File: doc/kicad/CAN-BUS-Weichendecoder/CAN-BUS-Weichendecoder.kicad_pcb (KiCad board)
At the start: 2 copper layers, 25 parts, among them J1 RJ45_LED_Shielded, J2 RJ45_Shielded, K1 HFD2_005-S-L2-D, U1 ULN2803A, U2 ULN2803A, U3 PCF8574, U4 PCF8574, U5 PCF8574, U6 ULN2803A, U7 ULN2803A, U8 ULN2803A

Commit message: Aktueller Stand
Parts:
- moved K1 187.6 mm to (201.9, 52.1)
- moved U4 125.7 mm to (81.3, 100.3), turned to 90 degrees
- moved U7 106.4 mm to (99.1, 109.2), turned to 270 degrees
- moved C2 96.3 mm to (135.9, 95.3), turned to 270 degrees
- moved U5 84.9 mm to (111.8, 100.3), turned to 90 degrees
- moved U8 70.0 mm to (129.5, 109.2), turned to 270 degrees
- moved C1 55.8 mm to (77.5, 95.2), turned to 270 degrees
- moved U3 48.3 mm to (142.2, 100.3), turned to 90 degrees
- moved U6 46.9 mm to (160.0, 109.2), turned to 270 degrees
- moved JP2 46.2 mm to (92.7, 82.8)
- moved JP3 46.2 mm to (86.2, 82.8)
- moved JP4 46.2 mm to (89.5, 82.8)
- moved R2 46.2 mm to (87.6, 71.8)
- moved R1 46.2 mm to (91.2, 69.3)
- moved R3 46.2 mm to (87.6, 69.3)
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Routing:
- net GND: track 212.0 -> 320.7 mm
- net +5V: track 94.6 -> 165.5 mm
- net Net-(A1-Pad24): track 83.1 -> 139.2 mm
- net Net-(A1-Pad23): track 83.1 -> 136.7 mm
- net Net-(A1-Pad22): track 0.00 -> 40.7 mm
- net Net-(A1-Pad21): track 0.00 -> 40.7 mm
- net Net-(U3-Pad9): track 1.59 -> 32.1 mm
- net Net-(U3-Pad12): track 1.59 -> 20.7 mm
- net Net-(U3-Pad11): track 1.59 -> 20.7 mm
- net Net-(U3-Pad10): track 1.59 -> 20.7 mm
- net Net-(U3-Pad4): track 0.00 -> 18.9 mm
- net Net-(U3-Pad7): track 0.00 -> 16.8 mm
- net Net-(U3-Pad5): track 0.00 -> 11.0 mm
- net Net-(U3-Pad6): track 0.00 -> 8.89 mm
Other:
- board outline added: 158.8 x 124.5 mm

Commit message: Platine weiterentwickelt, aktueller Arbeitsstand
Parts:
- moved U6 17.0 mm to (175.3, 116.8)
- moved U3 10.8 mm to (149.9, 108.0)
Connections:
- A1 pad 13: Net-(A1-Pad13) -> (no net)
- A1 pad 14: Net-(A1-Pad14) -> (no net)
- A1 pad 15: Net-(A1-Pad15) -> (no net)
- A1 pad 16: Net-(A1-Pad16) -> (no net)
- A1 pad 5: Net-(A1-Pad5) -> (no net)
- Shield1 pad 1: +5V -> (no net)
- Shield1 pad 2: GND -> (no net)
- Shield1 pad 3: Net-(A1-Pad13) -> (no net)
- Shield1 pad 4: Net-(A1-Pad15) -> (no net)
- Shield1 pad 5: Net-(A1-Pad14) -> (no net)
- Shield1 pad 6: Net-(A1-Pad16) -> (no net)
- Shield1 pad 7: Net-(A1-Pad5) -> (no net)
- U6 pad 1: Net-(U3-Pad4) -> Net-(U3-Pad9)
- U6 pad 2: Net-(U3-Pad5) -> Net-(U3-Pad10)
- U6 pad 3: Net-(U3-Pad6) -> Net-(U3-Pad11)
- U6 pad 4: Net-(U3-Pad7) -> Net-(U3-Pad12)
- U6 pad 5: Net-(U3-Pad9) -> Net-(U3-Pad7)
- U6 pad 6: Net-(U3-Pad10) -> Net-(U3-Pad6)
- U6 pad 7: Net-(U3-Pad11) -> Net-(U3-Pad5)
- U6 pad 8: Net-(U3-Pad12) -> Net-(U3-Pad4)
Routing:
- net (no net): track 0.00 -> 197.6 mm
- net Net-(A1-Pad5): track 63.9 -> 0.00 mm
- net Net-(A1-Pad13): track 37.1 -> 0.00 mm
- net Net-(A1-Pad14): track 35.2 -> 0.00 mm
- net Net-(A1-Pad15): track 30.9 -> 0.00 mm
- net Net-(A1-Pad16): track 26.7 -> 0.00 mm
- net GND: track 320.7 -> 303.4 mm
- net Net-(U3-Pad4): track 18.9 -> 8.89 mm
- net Net-(U3-Pad9): track 32.1 -> 23.4 mm
- net Net-(U3-Pad7): track 16.8 -> 8.89 mm
- net Net-(U3-Pad12): track 20.7 -> 27.7 mm
- net Net-(U3-Pad11): track 20.7 -> 27.7 mm
- net Net-(U3-Pad10): track 20.7 -> 25.9 mm
- net Net-(U3-Pad5): track 11.0 -> 8.89 mm

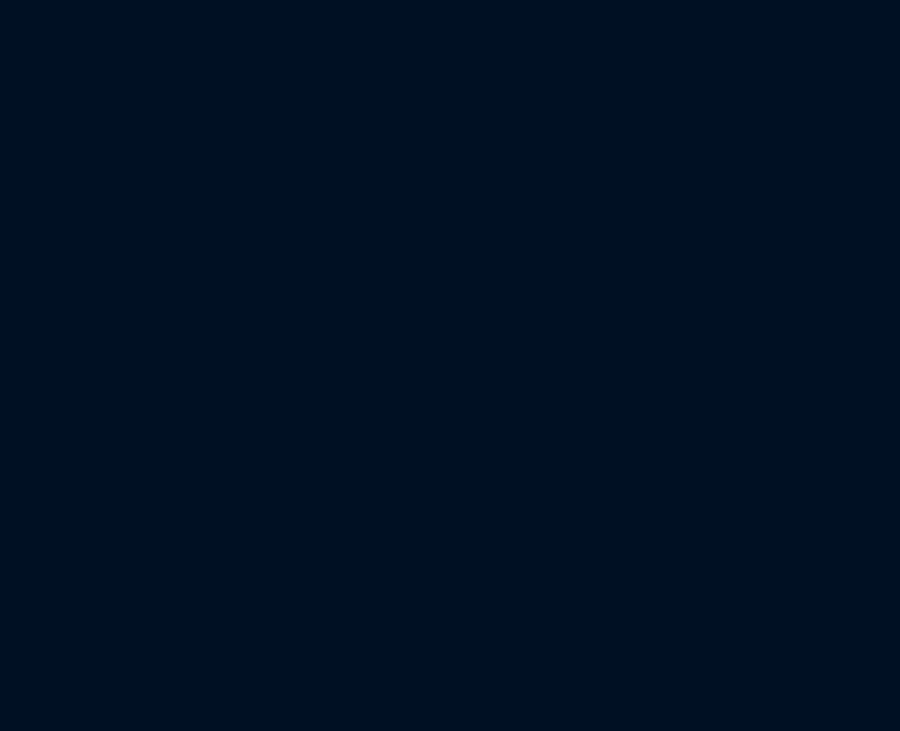
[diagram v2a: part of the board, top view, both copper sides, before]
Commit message: Auch die Bedruckung jetzt auf beiden Seiten, Platine jetzt komplett für Links und Rechts
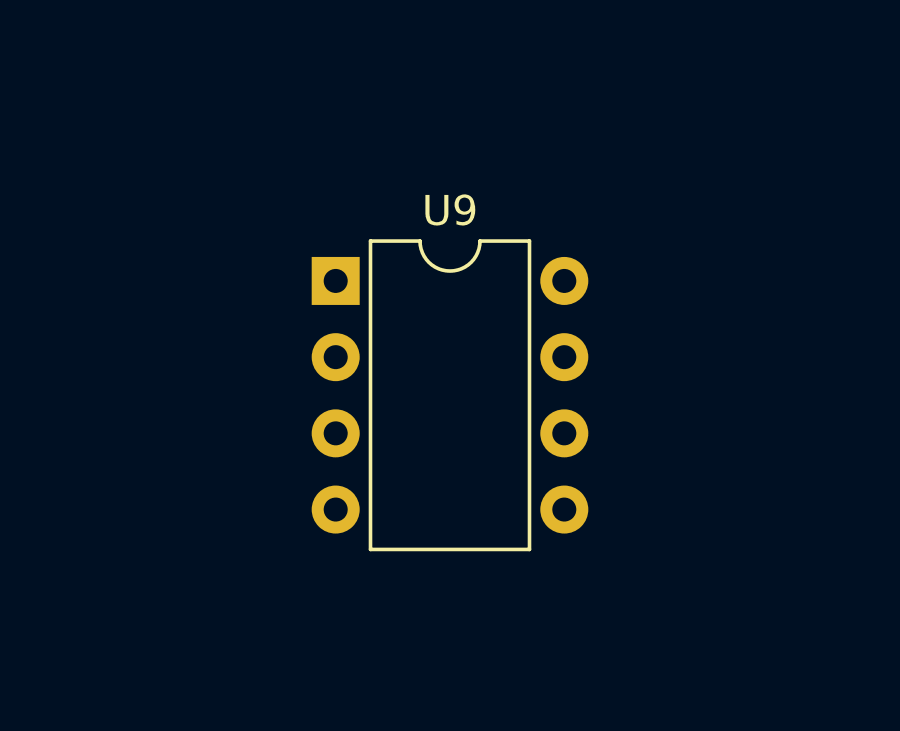
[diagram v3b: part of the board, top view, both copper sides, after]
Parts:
- added U9: 6N136, Package_DIP:DIP-8_W7.62mm, F.Cu at (39.4, 34.3)
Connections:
- A1 pad 6: (no net) -> Net-(A1-Pad6)

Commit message: Wago-Klemmen 250-140x verwendet
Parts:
- removed K1: HFD2_005-S-L2-D, HFD2_005-S-L2-D:HFD2005SL2D
- removed Shield1: CAN-BUS_MODULE_TJA1050, kicad-lib:MCP2515_CAN_MODULE_BY0-10
- removed the U9 at (39.4, 34.3)
- added C1: 2200µ/35V, Capacitors_THT:CP_Radial_D16.0mm_P7.50mm, F.Cu at (-199.9, -160.5)
- added C2: 2200µF/35V, Capacitors_THT:CP_Radial_D16.0mm_P7.50mm, F.Cu at (-217.6, -160.5)
- added D1: 1N4004, Diodes_THT:D_DO-15_P10.16mm_Horizontal, F.Cu at (-31.5, -114.7)
- added D2: B40C1500A, Diodes_THT:Diode_Bridge_DIP-4_W7.62mm_P5.08mm, F.Cu at (-17.8, -114.8)
- added D3: B140C1000A, Diodes_THT:Diode_Bridge_DIP-4_W7.62mm_P5.08mm, F.Cu at (15.7, -67.3)
- added DS1001: DC-10SGWA, Kingbright-LED:DIPS750W80P254L2540H825Q20N, F.Cu at (160.0, 55.9)
- added J1: 250-1404, Wago:250-1404, F.Cu at (76.2, 3.81)
- added J1001: Conn_01x02_Female, Pin_Headers:Pin_Header_Straight_1x02_Pitch2.54mm, F.Cu at (223.5, 72.4)
- added J1003: Conn_01x07_Female, Pin_Headers:Pin_Header_Straight_1x07_Pitch2.54mm, F.Cu at (69.8, 58.4)
- added J11: 250-1406, Wago:CONN_250-1406_WAG, F.Cu at (124.5, 129.5)
- added J12: Wago 250-1406, Wago:CONN_250-1406_WAG, F.Cu at (104.1, 129.5)
- added J13: Wago 250-1406, Wago:CONN_250-1406_WAG, F.Cu at (83.8, 129.5)
- added J14: Wago 250-1406, Wago:CONN_250-1406_WAG, F.Cu at (63.5, 129.5)
- added J2: 250-1404, Wago:250-1404, F.Cu at (88.9, 3.81)
- added J3: 250-1404, Wago:250-1404, F.Cu at (101.6, 3.81)
- added J31: 2604-1102, CONN_2604-1102_4_WAG, F.Cu at (-191.8, 14.6)
- added J4: 250-1404, Wago:250-1404, F.Cu at (114.3, 3.81)
- added J41: 2604-1102, CONN_2604-1102_4_WAG, F.Cu at (-175.8, 14.6)
- added J5: 250-1404, Wago:250-1404, F.Cu at (127.0, 3.81)
- added JP1: JP3, Pin_Headers:Pin_Header_Straight_1x02_Pitch2.54mm, F.Cu at (92.7, 82.8)
- added JP11: Jumper, Pin_Headers:Pin_Header_Straight_1x02_Pitch2.54mm, F.Cu at (219.7, 36.8)
- added R1: 1k5, Resistors_THT:R_Axial_DIN0207_L6.3mm_D2.5mm_P7.62mm_Horizontal, F.Cu at (4.89, -60.3)
- added R2: 10K, Resistors_THT:R_Axial_DIN0207_L6.3mm_D2.5mm_P7.62mm_Horizontal, F.Cu at (15.7, -72.0)
- added R7: 1k, Resistors_THT:R_Array_SIP6, F.Cu at (175.3, 53.3)
- added R8: 1k, Resistors_THT:R_Array_SIP6, F.Cu at (175.3, 81.3)
- added Shield1001: CAN-BUS_MODULE_TJA1050, CAN-BUS-MODULE:MCP2515_CAN_MODULE_BY0-10, F.Cu at (67.3, 52.1)
- added U10: TSR_1-24120, Converters_DCDC_ACDC:DCDC-Conv_TRACO_TSR-1, F.Cu at (-218.4, -145.3)
- added U1001: 6N136, Package_DIP:DIP-8_W7.62mm, F.Cu at (4.94, -72.1)
- added U11: TSR_1-2450, Converters_DCDC_ACDC:DCDC-Conv_TRACO_TSR-1, F.Cu at (-205.0, -145.3)
- J22: renamed from J2; value RJ45_Shielded -> J22
- JP2: value JP3 -> JP1; footprint Connectors:GS2 -> Pin_Headers:Pin_Header_Straight_1x02_Pitch2.54mm
- JP3: value JP1 -> JP2; footprint Connectors:GS2 -> Pin_Headers:Pin_Header_Straight_1x02_Pitch2.54mm
- JP4: value JP2 -> Jumper; footprint Connectors:GS2 -> Pin_Headers:Pin_Header_Straight_1x02_Pitch2.54mm
- moved JP4 264.2 mm to (-115.6, -83.8)
- moved U9 58.4 mm to (71.1, 109.2)
- moved U7 48.9 mm to (127.0, 109.2)
- moved U6 46.6 mm to (66.0, 91.4), turned to 270 degrees
- moved U4 41.6 mm to (109.2, 99.1)
- moved C1002 14.0 mm to (149.9, 94.0)
- moved R1007 11.6 mm to (134.6, 83.8)
- moved R1008 10.2 mm to (133.3, 90.2)
- moved JP2 6.50 mm to (86.2, 82.8)
- moved C1001 6.48 mm to (71.1, 94.0)
- moved C1003 4.04 mm to (101.6, 94.0)
- moved JP3 3.25 mm to (89.5, 82.8)
- moved U5 2.84 mm to (78.7, 99.1)
- renumbered C1 to C1001, C2 to C1002, C3 to C1003, J1 to J21, R4 to R1007, R5 to R1008, R6 to R3, R1 to R4, R3 to R5, R2 to R6, A1 to U1, U1 to U2, U2 to U3, U3 to U4, U4 to U5, U5 to U6, U6 to U7, U7 to U8, U8 to U9
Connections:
- JP2 pad 1: Net-(A1-Pad25) -> Net-(JP2-Pad1)
- JP4 pad 2: GND -> +12V
- R4 pad 1: Net-(A1-Pad25) -> Net-(JP1-Pad1)
- R4 pad 2: Net-(JP3-Pad1) -> Net-(JP2-Pad1)
- R5 pad 1: Net-(A1-Pad25) -> Net-(JP1-Pad1)
- R5 pad 2: Net-(JP4-Pad1) -> Net-(JP3-Pad1)
- R6 pad 2: Net-(A1-Pad25) -> Net-(JP1-Pad1)
- U1 pad 13: (no net) -> Net-(J1003-Pad3)
- U1 pad 14: (no net) -> Net-(J1003-Pad5)
- U1 pad 15: (no net) -> Net-(J1003-Pad4)
- U1 pad 16: (no net) -> Net-(J1003-Pad6)
- U1 pad 25: Net-(A1-Pad25) -> Net-(JP1-Pad1)
- U1 pad 5: (no net) -> Net-(J1003-Pad7)
- U2 pad 10: (no net) -> Net-(JP4-Pad1)
- U2 pad 11: (no net) -> Net-(J4-Pad3)
- U2 pad 12: (no net) -> Net-(J4-Pad2)
- U2 pad 13: (no net) -> Net-(J3-Pad3)
- U2 pad 14: (no net) -> Net-(J3-Pad2)
- U2 pad 15: (no net) -> Net-(J2-Pad3)
- U2 pad 16: (no net) -> Net-(J2-Pad2)
- U2 pad 17: (no net) -> Net-(J1-Pad3)
- U2 pad 18: (no net) -> Net-(J1-Pad2)
- U3 pad 10: (no net) -> Net-(JP4-Pad1)
- U3 pad 17: (no net) -> Net-(J5-Pad3)
- U3 pad 18: (no net) -> Net-(J5-Pad2)
- U7 pad 11: (no net) -> Net-(J12-Pad3)
- U7 pad 12: (no net) -> Net-(J12-Pad4)
- U7 pad 13: (no net) -> Net-(J12-Pad5)
- U7 pad 14: (no net) -> Net-(J11-Pad1)
- U7 pad 15: (no net) -> Net-(J11-Pad2)
- U7 pad 16: (no net) -> Net-(J11-Pad3)
- U7 pad 17: (no net) -> Net-(J11-Pad4)
- U7 pad 18: (no net) -> Net-(J11-Pad5)
- U8 pad 11: (no net) -> Net-(J14-Pad5)
- U8 pad 12: (no net) -> Net-(J13-Pad1)
- U8 pad 13: (no net) -> Net-(J13-Pad2)
- U8 pad 14: (no net) -> Net-(J13-Pad3)
- U8 pad 15: (no net) -> Net-(J13-Pad4)
- U8 pad 16: (no net) -> Net-(J13-Pad5)
- U8 pad 17: (no net) -> Net-(J12-Pad1)
- U8 pad 18: (no net) -> Net-(J12-Pad2)
- U9 pad 15: (no net) -> Net-(J14-Pad1)
- U9 pad 16: (no net) -> Net-(J14-Pad2)
- U9 pad 17: (no net) -> Net-(J14-Pad3)
- U9 pad 18: (no net) -> Net-(J14-Pad4)
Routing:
- net (no net): track 197.6 -> 0.00 mm
- net GND: track 303.4 -> 145.5 mm
- net Net-(R1007-Pad1): track 139.2 -> 0.00 mm
- net Net-(R1008-Pad1): track 136.7 -> 0.00 mm
- net +5V: track 165.5 -> 69.8 mm
- net Net-(J1003-Pad7): track 0.00 -> 52.5 mm
- net Net-(J1003-Pad3): track 0.00 -> 37.1 mm
- net Net-(J1003-Pad5): track 0.00 -> 35.2 mm
- net Net-(U6-Pad9): track 31.3 -> 0.00 mm
- net Net-(J1003-Pad4): track 0.00 -> 30.9 mm
- net Net-(U5-Pad9): track 30.6 -> 0.00 mm
- net Net-(U4-Pad12): track 27.7 -> 0.00 mm
- net Net-(U4-Pad11): track 27.7 -> 0.00 mm
- net Net-(U4-Pad10): track 25.9 -> 0.00 mm
- net Net-(U4-Pad9): track 23.4 -> 0.00 mm
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
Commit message: PCP weiterentwickelt
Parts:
- removed C1002: 100n, Capacitors_THT:C_Disc_D7.0mm_W2.5mm_P5.00mm
- removed J21: RJ45_LED_Shielded, Connectors:RJ45_TRANSFO
- removed R1007, R1008: 4k7, Resistors_SMD:R_0603
- removed R3: 1K, Resistors_SMD:R_0603
- added C4: 100n, Capacitors_THT:C_Disc_D7.0mm_W2.5mm_P5.00mm, F.Cu at (99.1, 92.7)
- added J15: Wago 250-1406, Wago:CONN_250-1406_WAG, F.Cu at (160.0, 127.0)
- added J23: J22, ASSMANN_WSW:A20042LPFS, F.Cu at (41.9, 127.0)
- added JP23: 12V CAN, Pin_Headers:Pin_Header_Straight_1x02_Pitch2.54mm, F.Cu at (57.1, 133.3)
- added JP41: DCC B, Pin_Headers:Pin_Header_Straight_1x02_Pitch2.54mm, F.Cu at (40.6, 90.2)
- added JP42: DCC A, Pin_Headers:Pin_Header_Straight_1x02_Pitch2.54mm, F.Cu at (44.5, 90.2)
- added R7: 4k7, Resistors_THT:R_Axial_DIN0207_L6.3mm_D2.5mm_P7.62mm_Horizontal, F.Cu at (114.3, 83.8)
- added R8: 4k7, Resistors_THT:R_Axial_DIN0207_L6.3mm_D2.5mm_P7.62mm_Horizontal, F.Cu at (114.3, 80.0)
- J22: footprint Connectors:RJ45_8 -> ASSMANN_WSW:A20042LPFS
- JP1: value JP3 -> Prog 1
- JP2: value JP1 -> Prog2
- JP3: value JP2 -> Prog3
- R4, R5, R6: footprint Resistors_SMD:R_0603 -> Resistors_THT:R_Axial_DIN0207_L6.3mm_D2.5mm_P7.62mm_Horizontal
- moved D3 265.2 mm to (-237.5, -146.1), turned to 270 degrees
- moved D2 224.6 mm to (-237.5, -161.3), turned to 270 degrees
- moved J31 183.3 mm to (-251.5, -158.8), turned to 270 degrees
- moved J22 97.6 mm to (41.9, 105.4)
- moved U9 94.0 mm to (165.1, 106.7)
- moved J14 76.2 mm to (139.7, 127.0)
- moved U6 71.5 mm to (137.2, 99.1), turned to 90 degrees
- moved C6 61.0 mm to (132.1, 92.7)
- moved D1 51.3 mm to (-2.54, -72.4), turned to 270 degrees
- moved J11 45.8 mm to (78.7, 127.0)
- moved U4 38.1 mm to (71.1, 99.1)
- moved J13 35.7 mm to (119.4, 127.0)
- moved C5 35.6 mm to (66.0, 92.7)
- moved U8 33.1 mm to (132.1, 106.7)
- moved U7 28.1 mm to (99.1, 106.7)
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- renumbered C1 to C10, C2 to C11, C1003 to C5, C1001 to C6, R8 to R10, R7 to R9
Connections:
- J11 pad 1: Net-(J11-Pad1) -> +5V
- J11 pad 6: +5V -> Net-(J11-Pad6)
- J12 pad 1: Net-(J12-Pad1) -> +5V
- J12 pad 6: +5V -> Net-(J12-Pad6)
- J13 pad 1: Net-(J13-Pad1) -> +5V
- J13 pad 6: +5V -> Net-(J13-Pad6)
- J14 pad 1: Net-(J14-Pad1) -> +5V
- J14 pad 6: +5V -> Net-(J14-Pad6)
- J22 pad 1: Net-(J21-Pad1) -> Net-(J22-Pad1)
- J22 pad 2: Net-(J21-Pad2) -> Net-(J22-Pad2)
- J22 pad 4: Net-(J21-Pad4) -> GND
- J22 pad 7: GND -> Net-(J22-Pad7)
- J22 pad 8: +5V -> Net-(J22-Pad8)
- J31 pad 1: Net-(D2-Pad3) -> Net-(D2-Pad2)
- J31 pad 2: Net-(D2-Pad3) -> Net-(D2-Pad2)
- J31 pad 3: Net-(D2-Pad2) -> Net-(D2-Pad3)
- J31 pad 4: Net-(D2-Pad2) -> Net-(D2-Pad3)
- J41 pad 1: Net-(D1-Pad2) -> Net-(J41-Pad1)
- J41 pad 2: Net-(D1-Pad2) -> Net-(J41-Pad1)
- J41 pad 3: Net-(J41-Pad3) -> Net-(D1-Pad2)
- J41 pad 4: Net-(J41-Pad3) -> Net-(D1-Pad2)
- R1 pad 2: Net-(J41-Pad3) -> Net-(J41-Pad1)
- Shield1001 pad H: Net-(J21-Pad1) -> Net-(J22-Pad8)
- Shield1001 pad L: Net-(J21-Pad2) -> Net-(J22-Pad7)
- U7 pad 1: Net-(U4-Pad9) -> Net-(U4-Pad12)
- U7 pad 11: Net-(J12-Pad3) -> Net-(J11-Pad2)
- U7 pad 12: Net-(J12-Pad4) -> Net-(J11-Pad3)
- U7 pad 13: Net-(J12-Pad5) -> Net-(J11-Pad4)
- U7 pad 14: Net-(J11-Pad1) -> Net-(J11-Pad5)
- U7 pad 15: Net-(J11-Pad2) -> Net-(J11-Pad6)
- U7 pad 16: Net-(J11-Pad3) -> Net-(J12-Pad2)
- U7 pad 17: Net-(J11-Pad4) -> Net-(J12-Pad3)
- U7 pad 18: Net-(J11-Pad5) -> Net-(J12-Pad4)
- U7 pad 2: Net-(U4-Pad10) -> Net-(U4-Pad11)
- U7 pad 3: Net-(U4-Pad11) -> Net-(U4-Pad10)
- U7 pad 4: Net-(U4-Pad12) -> Net-(U4-Pad9)
- U8 pad 1: Net-(U5-Pad4) -> Net-(U5-Pad12)
- U8 pad 11: Net-(J14-Pad5) -> Net-(J12-Pad5)
- U8 pad 12: Net-(J13-Pad1) -> Net-(J12-Pad6)
- U8 pad 17: Net-(J12-Pad1) -> Net-(J13-Pad6)
- U8 pad 18: Net-(J12-Pad2) -> Net-(J14-Pad2)
- U8 pad 2: Net-(U5-Pad5) -> Net-(U5-Pad11)
- U8 pad 3: Net-(U5-Pad6) -> Net-(U5-Pad10)
- U8 pad 4: Net-(U5-Pad7) -> Net-(U5-Pad9)
- U8 pad 5: Net-(U5-Pad9) -> Net-(U5-Pad7)
- U8 pad 6: Net-(U5-Pad10) -> Net-(U5-Pad6)
- U8 pad 7: Net-(U5-Pad11) -> Net-(U5-Pad5)
- U8 pad 8: Net-(U5-Pad12) -> Net-(U5-Pad4)
- U9 pad 1: Net-(U6-Pad4) -> Net-(U6-Pad12)
- U9 pad 11: (no net) -> Net-(J14-Pad3)
- U9 pad 12: (no net) -> Net-(J14-Pad4)
- U9 pad 13: (no net) -> Net-(J14-Pad5)
- U9 pad 14: (no net) -> Net-(J14-Pad6)
- U9 pad 15: Net-(J14-Pad1) -> Net-(J15-Pad2)
- U9 pad 16: Net-(J14-Pad2) -> Net-(J15-Pad3)
- U9 pad 17: Net-(J14-Pad3) -> Net-(J15-Pad4)
- U9 pad 18: Net-(J14-Pad4) -> Net-(J15-Pad5)
- U9 pad 2: Net-(U6-Pad5) -> Net-(U6-Pad11)
- U9 pad 3: Net-(U6-Pad6) -> Net-(U6-Pad10)
- U9 pad 4: Net-(U6-Pad7) -> Net-(U6-Pad9)
- U9 pad 5: Net-(U6-Pad9) -> Net-(U6-Pad7)
- U9 pad 6: Net-(U6-Pad10) -> Net-(U6-Pad6)
- U9 pad 7: Net-(U6-Pad11) -> Net-(U6-Pad5)
- U9 pad 8: Net-(U6-Pad12) -> Net-(U6-Pad4)
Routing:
- net GND: track 145.5 -> 450.3 mm
- net +5V: track 69.8 -> 230.7 mm
- net Net-(J22-Pad7): track 0.00 -> 103.2 mm, vias 0 -> 1
- net Net-(R7-Pad1): track 0.00 -> 100.0 mm
- net Net-(R8-Pad1): track 0.00 -> 99.2 mm
- net Net-(J22-Pad8): track 0.00 -> 91.2 mm, vias 0 -> 1
- net Net-(J22-Pad2): track 0.00 -> 61.9 mm, vias 0 -> 1
- net Net-(DS1001-Pad6): track 8.89 -> 70.8 mm
- net +12V: track 0.00 -> 61.9 mm
- net Net-(J22-Pad1): track 0.00 -> 60.8 mm, vias 0 -> 1
- net Net-(DS1001-Pad7): track 26.2 -> 86.0 mm
- net Net-(DS1001-Pad5): track 8.89 -> 67.2 mm
- net Net-(DS1001-Pad4): track 8.89 -> 63.6 mm
- net Net-(DS1001-Pad3): track 8.89 -> 60.0 mm
- net Net-(JP1-Pad1): track 0.00 -> 49.6 mm
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
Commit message: Erster kompletter Entwurf der Platine
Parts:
- removed C10: 2200µ/35V, Capacitors_THT:CP_Radial_D16.0mm_P7.50mm
- removed C11: 2200µF/35V, Capacitors_THT:CP_Radial_D16.0mm_P7.50mm
- removed D2: B40C1500A, Diodes_THT:Diode_Bridge_DIP-4_W7.62mm_P5.08mm
- removed D3: B140C1000A, Diodes_THT:Diode_Bridge_DIP-4_W7.62mm_P5.08mm
- removed U11: TSR_1-2450, Converters_DCDC_ACDC:DCDC-Conv_TRACO_TSR-1
- added D1001: DIODE, Diodes_THT:D_DO-15_P10.16mm_Horizontal, F.Cu at (77.5, 71.1)
- added D1002: LED, LEDs:LED_D3.0mm, F.Cu at (105.4, 74.9)
- added R20: 470, Resistors_THT:R_Axial_DIN0207_L6.3mm_D2.5mm_P7.62mm_Horizontal, F.Cu at (100.3, 72.4)
- J1003, Shield1001: moved to B.Cu
- J31: value 2604-1102 -> 12V DC
- U10: value TSR_1-24120 -> TSR_1-2450
- moved J31 395.5 mm to (68.6, 73.7)
- moved U10 374.7 mm to (87.6, 74.9)
- moved JP4 345.4 mm to (196.8, 63.5), turned to 270 degrees
- moved J41 247.8 mm to (68.6, 55.9), turned to 270 degrees
- moved JP11 170.3 mm to (73.7, 124.5)
- moved J1001 164.9 mm to (64.8, 116.8), turned to 90 degrees
- moved R2 159.3 mm to (102.9, 57.1)
- moved U1001 156.4 mm to (88.9, 57.1)
- moved D1 153.6 mm to (83.8, 54.6)
- moved R1 152.9 mm to (77.5, 54.6), turned to 270 degrees
- moved JP1 101.9 mm to (176.5, 115.6), turned to 90 degrees
- moved JP3 99.2 mm to (176.5, 111.8), turned to 90 degrees
- moved JP2 97.0 mm to (176.5, 108.0), turned to 90 degrees
- moved R5 75.6 mm to (163.8, 111.8), turned to 0 degrees
- moved Shield1001 72.7 mm to (97.8, 118.1), turned to 90 degrees
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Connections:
- J31 pad 1: Net-(D2-Pad2) -> +12V
- J31 pad 2: Net-(D2-Pad2) -> +12V
- J31 pad 3: Net-(D2-Pad3) -> GND
- J31 pad 4: Net-(D2-Pad3) -> GND
- J41 pad 1: Net-(J41-Pad1) -> Net-(D1-Pad2)
- J41 pad 2: Net-(J41-Pad1) -> Net-(D1-Pad2)
- J41 pad 3: Net-(D1-Pad2) -> Net-(J41-Pad3)
- J41 pad 4: Net-(D1-Pad2) -> Net-(J41-Pad3)
- JP23 pad 2: +12V -> Net-(D1001-Pad2)
- JP42 pad 1: Net-(J41-Pad1) -> Net-(J41-Pad3)
- R1 pad 2: Net-(J41-Pad1) -> Net-(J41-Pad3)
- U10 pad 1: Net-(C10-Pad1) -> Net-(D1001-Pad2)
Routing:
- net GND: track 450.3 -> 611.2 mm
- net +5V: track 230.7 -> 372.1 mm, vias 0 -> 1
- net +12V: track 61.9 -> 170.6 mm
- net Net-(D1-Pad2): track 13.0 -> 112.2 mm
- net Net-(J41-Pad3): track 0.00 -> 84.7 mm
- net Net-(D1001-Pad2): track 0.00 -> 80.0 mm
- net Net-(R2-Pad2): track 5.08 -> 79.0 mm, vias 0 -> 1
- net Net-(DS1001-Pad8): track 26.2 -> 83.9 mm
- net Net-(J1003-Pad6): track 0.00 -> 35.9 mm
- net Net-(C10-Pad1): track 34.3 -> 0.00 mm
- net Net-(D2-Pad2): track 31.9 -> 0.00 mm
- net Net-(J1003-Pad3): track 37.1 -> 63.8 mm
- net Net-(J1003-Pad4): track 30.9 -> 56.9 mm
- net Net-(DS1001-Pad10): track 54.3 -> 75.9 mm, vias 0 -> 1
- net Net-(DS1001-Pad9): track 57.5 -> 77.9 mm, vias 0 -> 1
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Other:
- net class Power added: clearance 0.5, trace_width 1, via_dia 0.8, via_drill 0.4
